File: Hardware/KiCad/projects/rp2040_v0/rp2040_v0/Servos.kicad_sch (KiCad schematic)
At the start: 24 parts, among them J15 Conn_01x03, J16 Conn_01x03, J17 Conn_01x03, J18 Conn_01x03, J19 Conn_01x03, J20 Conn_01x03, J21 Conn_01x03, U10 TXS0108EPWR, U7 AMS1117-5.0, U8 AMS1117-5.0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

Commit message: Remove level shifter from design
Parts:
- removed C30, C31: 100nF, Capacitor_SMD:C_0402_1005Metric, symbol Device:C_Small
- removed J15, J16: Conn_01x03, Connector_PinHeader_2.54mm:PinHeader_1x03_P2.54mm_Vertical, symbol Connector_Generic:Conn_01x03
- removed R27, R28, R29, R30, R31: 0 ohm, Resistor_SMD:R_0402_1005Metric, symbol Device:R_Small
- removed U10: TXS0108EPWR, easyeda2kicad:TSSOP-20_L6.5-W4.4-P0.65-LS6.4-BL, symbol easyeda2kicad:TXS0108EPWR
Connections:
- net PWM_0_A__Servo_A: now also J21.1 (Pin_1)
- net PWM_1_A__Servo_B: now also J20.1 (Pin_1)
- net PWM_2_B__Servo_C: now also J19.1 (Pin_1)
- net PWM_3_A__Servo_D: now also J18.1 (Pin_1)
- net PWM_4_A__Servo_E: now also J17.1 (Pin_1)
- net 5v_Servo_E_and_level_shifter renamed 5v_Servo_E
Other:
- note removed: "I've been lead to believe all servos can handle 3.3v signals and a level shifter is not needed. Do not populate the level shifter. Add later if needed and remove the 0 ohm resistor."

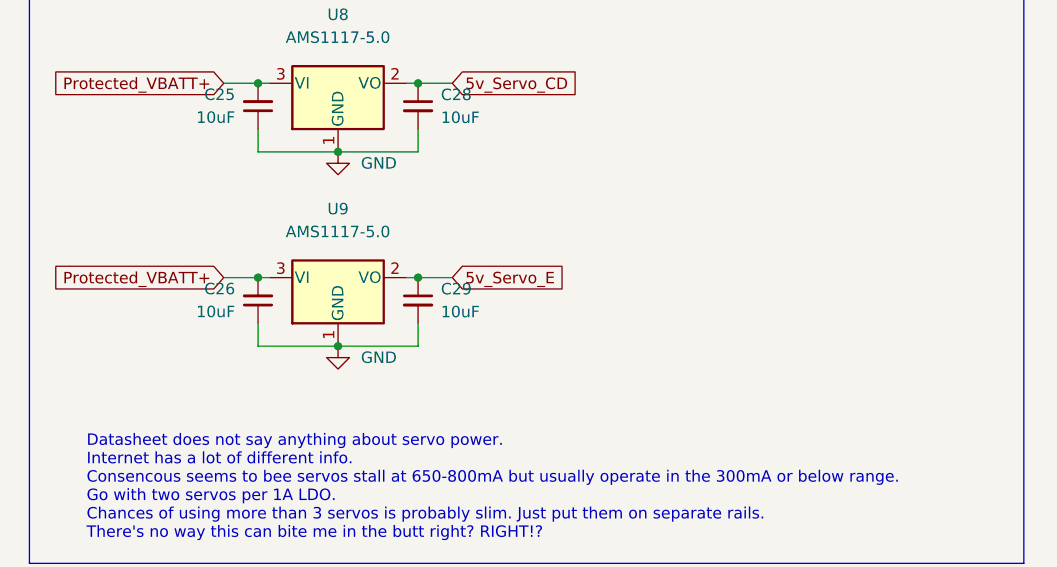
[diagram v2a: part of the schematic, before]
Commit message: Remove extra servo LDO. Nothing else is on that 5V rail so share the normal one.
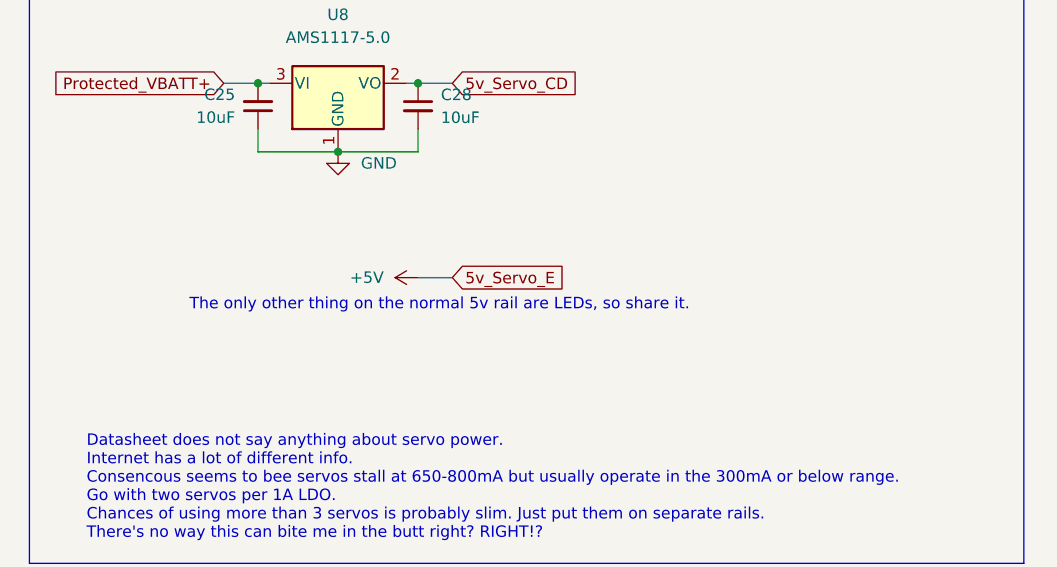
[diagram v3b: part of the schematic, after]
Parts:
- removed C26, C29: 10uF, Capacitor_SMD:C_0805_2012Metric, symbol Device:C_Small
- removed U9: AMS1117-5.0, Package_TO_SOT_SMD:SOT-223-3_TabPin2, symbol Regulator_Linear:AMS1117-5.0
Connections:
- net 5v_Servo_E renamed +5V
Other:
- note added: "The only other thing on the normal 5v rail are LEDs, so share it."
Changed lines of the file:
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@@
     (rev "v0.1")
   )
-  (junction (at 46.99 172.72) (diameter 0) (color 0 0 0 0)
-  )
   (junction (at 46.99 151.13) (diameter 0) (color 0 0 0 0)
   )
   (junction (at 55.88 143.51) (diameter 0) (color 0 0 0 0)
   )
-  (junction (at 55.88 165.1) (diameter 0) (color 0 0 0 0)
-  )
   (junction (at 46.99 129.54) (diameter 0) (color 0 0 0 0)
   )
@@
   (junction (at 38.1 143.51) (diameter 0) (color 0 0 0 0)
   )
-  (junction (at 38.1 165.1) (diameter 0) (color 0 0 0 0)
-  )
   (wire (pts (xy 55.88 121.92) (xy 54.61 121.92))
     (stroke (width 0) (type default) (color 0 0 0 0))
@@
     (stroke (width 0) (type default) (color 0 0 0 0))
   )
-  (wire (pts (xy 38.1 170.18) (xy 38.1 172.72))
-    (stroke (width 0) (type default) (color 0 0 0 0))
-  )
-  (wire (pts (xy 55.88 170.18) (xy 55.88 172.72))
-    (stroke (width 0) (type default) (color 0 0 0 0))
-  )
   (wire (pts (xy 167.64 95.25) (xy 171.45 95.25))
     (stroke (width 0) (type default) (color 0 0 0 0))
@@
     (stroke (width 0) (type default) (color 0 0 0 0))
   )
-  (wire (pts (xy 55.88 172.72) (xy 46.99 172.72))
-    (stroke (width 0) (type default) (color 0 0 0 0))
-  )
   (wire (pts (xy 238.76 44.45) (xy 238.76 71.12))
     (stroke (width 0) (type default) (color 0 0 0 0))
@@
     (stroke (width 0) (type default) (color 0 0 0 0))
   )
-  (wire (pts (xy 38.1 172.72) (xy 46.99 172.72))
-    (stroke (width 0) (type default) (color 0 0 0 0))
-  )
   (wire (pts (xy 167.64 92.71) (xy 173.99 92.71))
     (stroke (width 0) (type default) (color 0 0 0 0))
@@
     (stroke (width 0) (type default) (color 0 0 0 0))
   )
-  (wire (pts (xy 54.61 165.1) (xy 55.88 165.1))
-    (stroke (width 0) (type default) (color 0 0 0 0))
-  )
   (wire (pts (xy 259.08 116.84) (xy 233.68 116.84))
     (stroke (width 0) (type default) (color 0 0 0 0))
@@
     (stroke (width 0) (type default) (color 0 0 0 0))
   )
-  (wire (pts (xy 38.1 165.1) (xy 39.37 165.1))
-    (stroke (width 0) (type default) (color 0 0 0 0))
-  )
   (wire (pts (xy 233.68 49.53) (xy 233.68 116.84))
-    (stroke (width 0) (type default) (color 0 0 0 0))
-  )
-  (wire (pts (xy 34.29 165.1) (xy 38.1 165.1))
     (stroke (width 0) (type default) (color 0 0 0 0))
   )
@@
     (effects (font (size 1.5 1.5) (thickness 0.3) bold) (justify left bottom))
   )
+  (text "The only other thing on the normal 5v rail are LEDs, so share it."
+    (at 30.48 168.91 0)
+    (effects (font (size 1.27 1.27)) (justify left bottom))
+  )
   (global_label "5v_Servo_CD" (shape input) (at 261.62 71.12 90) (fields_autoplaced)
     (effects (font (size 1.27 1.27)) (justify left))
@@
     (property "Intersheet References" "${INTERSHEET_REFS}" (id 0) (at 73.9564 143.4306 0)
       (effects (font (size 1.27 1.27)) (justify left) hide)
-    )
-  )
-  (global_label "Protected_VBATT+" (shape input) (at 34.29 165.1 180) (fields_autoplaced)
-    (effects (font (size 1.27 1.27)) (justify right))
-    (property "Intersheet References" "${INTERSHEET_REFS}" (id 0) (at 16.4555 165.1794 0)
-      (effects (font (size 1.27 1.27)) (justify right) hide)
     )
   )
@@
     (pin "1")
   )
-  (symbol (lib_id "Device:C_Small") (at 38.1 167.64 0) (mirror x) (unit 1)
+  (symbol (lib_id "Connector_Generic:Conn_01x03") (at 261.62 53.34 90) (mirror x) (unit 1)
+    (in_bom yes) (on_board yes)
+    (property "Reference" "J17" (id 0) (at 278.13 50.8 90)
+      (effects (font (size 1.27 1.27)) (justify left))
+    )
+    (property "Value" "Conn_01x03" (id 1) (at 278.13 53.34 90)
+      (effects (font (size 1.27 1.27)) (justify left))
+    )
+    (property "Footprint" "Connector_PinHeader_2.54mm:PinHeader_1x03_P2.54mm_Vertical" (id 2) (at 261.62 53.34 0)
+      (effects (font (size 1.27 1.27)) hide)
+    )
+    (property "Datasheet" "~" (id 3) (at 261.62 53.34 0)
+      (effects (font (size 1.27 1.27)) hide)
+    )
+    (pin "1")
+    (pin "2")
+    (pin "3")
+  )
+  (symbol (lib_id "Connector_Generic:Conn_01x03") (at 261.62 76.2 90) (mirror x) (unit 1)
+    (in_bom yes) (on_board yes)
+    (property "Reference" "J18" (id 0) (at 278.13 73.66 90)
+      (effects (font (size 1.27 1.27)) (justify left))
+    )
+    (property "Value" "Conn_01x03" (id 1) (at 278.13 76.2 90)
+      (effects (font (size 1.27 1.27)) (justify left))
+    )
+    (property "Footprint" "Connector_PinHeader_2.54mm:PinHeader_1x03_P2.54mm_Vertical" (id 2) (at 261.62 76.2 0)
+      (effects (font (size 1.27 1.27)) hide)
+    )
+    (property "Datasheet" "~" (id 3) (at 261.62 76.2 0)
+      (effects (font (size 1.27 1.27)) hide)
+    )
+    (pin "1")
+    (pin "2")
+    (pin "3")
+  )
+  (symbol (lib_id "power:+5V") (at 55.88 165.1 90) (unit 1)
     (in_bom yes) (on_board yes) (fields_autoplaced)
-    (property "Reference" "C26" (id 0) (at 35.56 166.3635 0)
-      (effects (font (size 1.27 1.27)) (justify right))
-    )
-    (property "Value" "10uF" (id 1) (at 35.56 168.9035 0)
-      (effects (font (size 1.27 1.27)) (justify right))
-    )
-    (property "Footprint" "Capacitor_SMD:C_0805_2012Metric" (id 2) (at 38.1 167.64 0)
-      (effects (font (size 1.27 1.27)) hide)
-    )
-    (property "Datasheet" "~" (id 3) (at 38.1 167.64 0)
-      (effects (font (size 1.27 1.27)) hide)
-    )
-    (pin "1")
-    (pin "2")
-  )
-  (symbol (lib_id "Connector_Generic:Conn_01x03") (at 261.62 53.34 90) (mirror x) (unit 1)
-    (in_bom yes) (on_board yes)
-    (property "Reference" "J17" (id 0) (at 278.13 50.8 90)
-      (effects (font (size 1.27 1.27)) (justify left))
-    )
-    (property "Value" "Conn_01x03" (id 1) (at 278.13 53.34 90)
-      (effects (font (size 1.27 1.27)) (justify left))
-    )
-    (property "Footprint" "Connector_PinHeader_2.54mm:PinHeader_1x03_P2.54mm_Vertical" (id 2) (at 261.62 53.34 0)
-      (effects (font (size 1.27 1.27)) hide)
-    )
-    (property "Datasheet" "~" (id 3) (at 261.62 53.34 0)
-      (effects (font (size 1.27 1.27)) hide)
-    )
-    (pin "1")
-    (pin "2")
-    (pin "3")
-  )
-  (symbol (lib_id "Connector_Generic:Conn_01x03") (at 261.62 76.2 90) (mirror x) (unit 1)
-    (in_bom yes) (on_board yes)
-    (property "Reference" "J18" (id 0) (at 278.13 73.66 90)
-      (effects (font (size 1.27 1.27)) (justify left))
-    )
-    (property "Value" "Conn_01x03" (id 1) (at 278.13 76.2 90)
-      (effects (font (size 1.27 1.27)) (justify left))
-    )
-    (property "Footprint" "Connector_PinHeader_2.54mm:PinHeader_1x03_P2.54mm_Vertical" (id 2) (at 261.62 76.2 0)
-      (effects (font (size 1.27 1.27)) hide)
-    )
-    (property "Datasheet" "~" (id 3) (at 261.62 76.2 0)
-      (effects (font (size 1.27 1.27)) hide)
-    )
-    (pin "1")
-    (pin "2")
-    (pin "3")
-  )
-  (symbol (lib_id "Device:C_Small") (at 55.88 167.64 0) (mirror y) (unit 1)
-    (in_bom yes) (on_board yes) (fields_autoplaced)
-    (property "Reference" "C29" (id 0) (at 58.42 166.3762 0)
-      (effects (font (size 1.27 1.27)) (justify right))
-    )
-    (property "Value" "10uF" (id 1) (at 58.42 168.9162 0)
-      (effects (font (size 1.27 1.27)) (justify right))
-    )
-    (property "Footprint" "Capacitor_SMD:C_0805_2012Metric" (id 2) (at 55.88 167.64 0)
-      (effects (font (size 1.27 1.27)) hide)
-    )
-    (property "Datasheet" "~" (id 3) (at 55.88 167.64 0)
-      (effects (font (size 1.27 1.27)) hide)
-    )
-    (pin "1")
-    (pin "2")
+    (property "Reference" "#PWR?" (id 0) (at 59.69 165.1 0)
+      (effects (font (size 1.27 1.27)) hide)
+    )
+    (property "Value" "+5V" (id 1) (at 52.07 165.0999 90)
+      (effects (font (size 1.27 1.27)) (justify left))
+    )
+    (property "Footprint" "" (id 2) (at 55.88 165.1 0)
+      (effects (font (size 1.27 1.27)) hide)
+    )
+    (property "Datasheet" "" (id 3) (at 55.88 165.1 0)
+      (effects (font (size 1.27 1.27)) hide)
+    )
+    (pin "1")
   )
   (symbol (lib_id "power:GND") (at 264.16 138.43 0) (mirror x) (unit 1)
@@
     (pin "1")
   )
-  (symbol (lib_id "power:GND") (at 46.99 172.72 0) (unit 1)
-    (in_bom yes) (on_board yes) (fields_autoplaced)
-    (property "Reference" "#PWR053" (id 0) (at 46.99 179.07 0)
-      (effects (font (size 1.27 1.27)) hide)
-    )
-    (property "Value" "GND" (id 1) (at 49.53 173.9899 0)
-      (effects (font (size 1.27 1.27)) (justify left))
-    )
-    (property "Footprint" "" (id 2) (at 46.99 172.72 0)
-      (effects (font (size 1.27 1.27)) hide)
-    )
-    (property "Datasheet" "" (id 3) (at 46.99 172.72 0)
-      (effects (font (size 1.27 1.27)) hide)
-    )
-    (pin "1")
-  )
-  (symbol (lib_id "Regulator_Linear:AMS1117-5.0") (at 46.99 165.1 0) (unit 1)
-    (in_bom yes) (on_board yes) (fields_autoplaced)
-    (property "Reference" "U9" (id 0) (at 46.99 157.48 0))
-    (property "Value" "AMS1117-5.0" (id 1) (at 46.99 160.02 0))
-    (property "Footprint" "Package_TO_SOT_SMD:SOT-223-3_TabPin2" (id 2) (at 46.99 160.02 0)
-      (effects (font (size 1.27 1.27)) hide)
-    )
-    (property "Datasheet" "http://www.advanced-monolithic.com/pdf/ds1117.pdf" (id 3) (at 49.53 171.45 0)
-      (effects (font (size 1.27 1.27)) hide)
-    )
-    (pin "1")
-    (pin "2")
-    (pin "3")
-  )
   (symbol (lib_id "power:GND") (at 46.99 151.13 0) (unit 1)

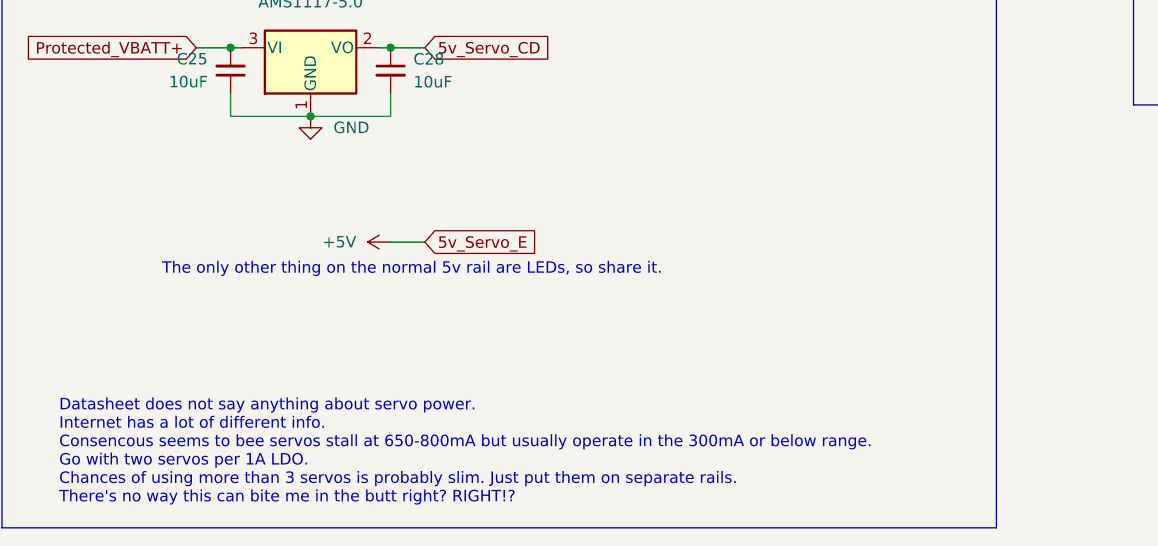
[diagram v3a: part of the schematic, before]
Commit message: Remove reaction wheel LDO. Add jumper to select power source.
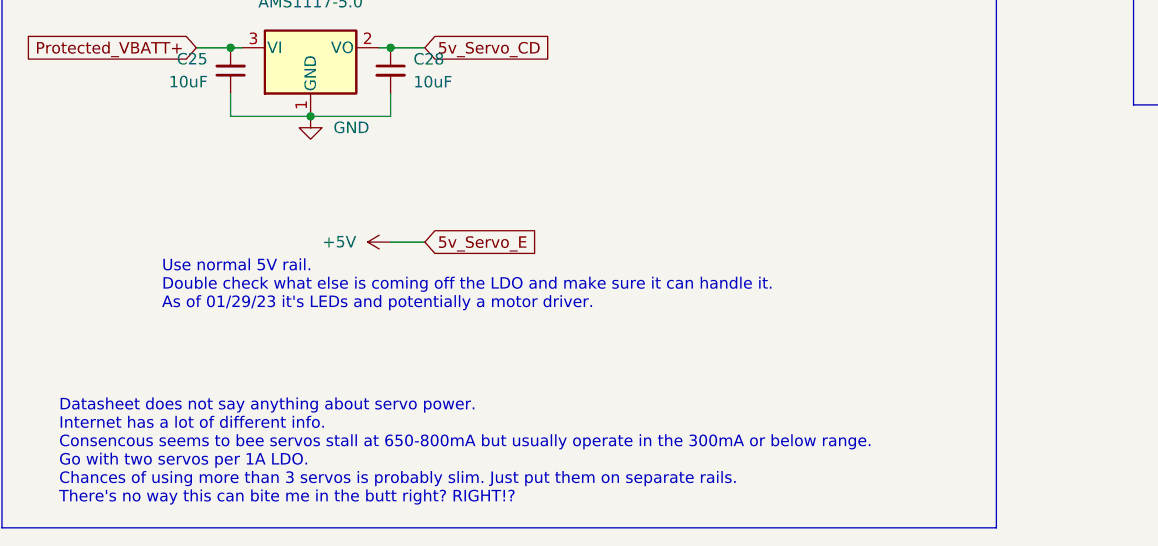
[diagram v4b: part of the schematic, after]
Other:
- note added: "Use normal 5V rail. Double check what else is coming off the LDO and make sure it can handle it. As of 01/29/23 it's LEDs and potentially a motor driver."
- note removed: "The only other thing on the normal 5v rail are LEDs, so share it."
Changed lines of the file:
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@@
     (effects (font (size 1.5 1.5) (thickness 0.3) bold) (justify left bottom))
   )
-  (text "The only other thing on the normal 5v rail are LEDs, so share it."
-    (at 30.48 168.91 0)
+  (text "Use normal 5V rail.\nDouble check what else is coming off the LDO and make sure it can handle it.\nAs of 01/29/23 it's LEDs and potentially a motor driver."
+    (at 30.48 172.72 0)
     (effects (font (size 1.27 1.27)) (justify left bottom))
   )
@@
   (symbol (lib_id "power:+5V") (at 55.88 165.1 90) (unit 1)
     (in_bom yes) (on_board yes) (fields_autoplaced)
-    (property "Reference" "#PWR?" (id 0) (at 59.69 165.1 0)
+    (property "Reference" "#PWR0105" (id 0) (at 59.69 165.1 0)
       (effects (font (size 1.27 1.27)) hide)
     )
